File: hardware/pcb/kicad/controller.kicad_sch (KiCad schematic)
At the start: 0 parts

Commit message: feat(hardware): complete reproducible engineering release artifacts
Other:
- note added: "AVL OWNER SIGN-OFF AND PHYSICAL BRING-UP REQUIRED BEFORE POPULATED-BOARD RELEASE"
- note added: "WORKBENCH-1 EVT CARRIER - ARCHITECTURE AND RELEASE GATES"
- note removed: "STOP: SYMBOL CAPTURE, AVL APPROVAL, ERC, ROUTING, DRC AND LAB VALIDATION REQUIRED"
- note removed: "WORKBENCH-1 CONTROLLER - ARCHITECTURE BASELINE - NOT FOR FABRICATION"
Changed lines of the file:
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@@
 (kicad_sch (version 20231120) (generator eeschema)
   (paper "A4")
-  (text "WORKBENCH-1 CONTROLLER - ARCHITECTURE BASELINE - NOT FOR FABRICATION"
+  (text "WORKBENCH-1 EVT CARRIER - ARCHITECTURE AND RELEASE GATES"
     (exclude_from_sim no) (at 105 20 0)
     (effects (font (size 2 2) (thickness 0.3)) (justify bottom)))
@@
     (exclude_from_sim no) (at 105 90 0)
     (effects (font (size 1.5 1.5) (thickness 0.25)) (justify bottom)))
-  (text "STOP: SYMBOL CAPTURE, AVL APPROVAL, ERC, ROUTING, DRC AND LAB VALIDATION REQUIRED"
+  (text "AVL OWNER SIGN-OFF AND PHYSICAL BRING-UP REQUIRED BEFORE POPULATED-BOARD RELEASE"
     (exclude_from_sim no) (at 105 115 0)
     (effects (font (size 1.25 1.25) (thickness 0.2)) (justify bottom)))

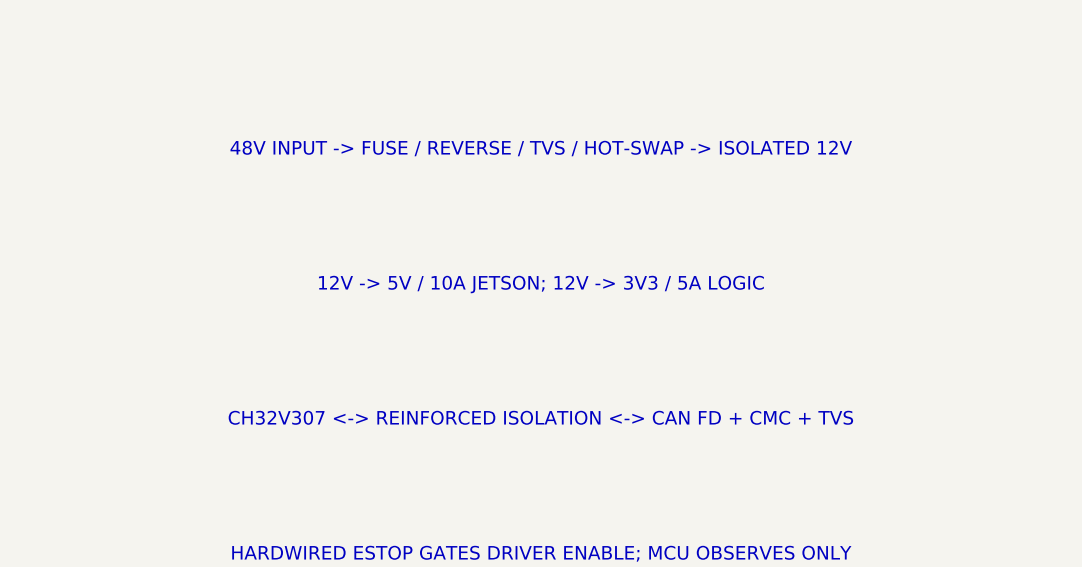
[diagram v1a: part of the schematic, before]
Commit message: feat(hardware): close EVT interface and isolation review
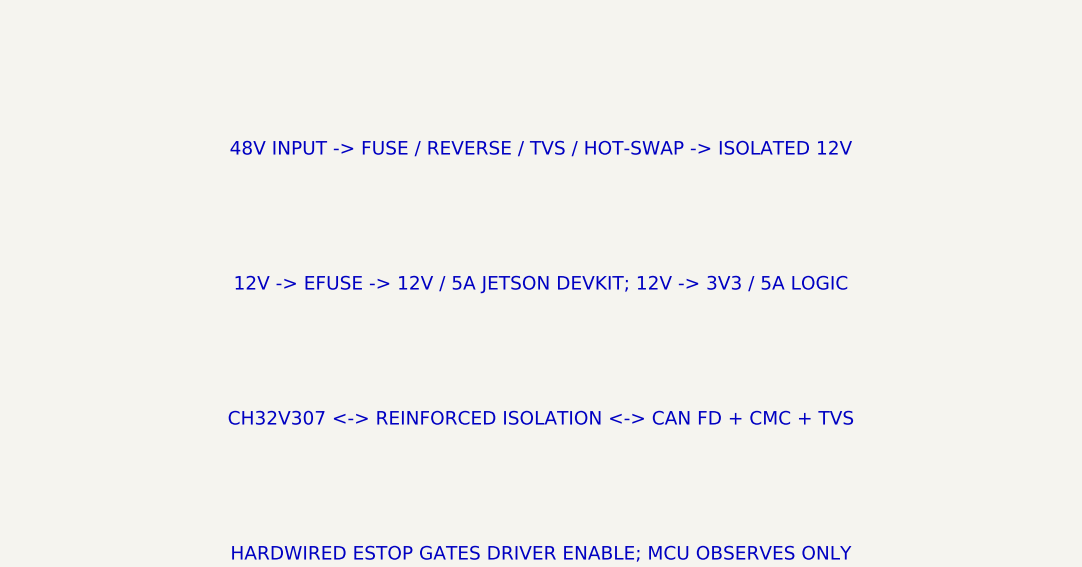
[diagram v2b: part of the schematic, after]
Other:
- note added: "12V -> EFUSE -> 12V / 5A JETSON DEVKIT; 12V -> 3V3 / 5A LOGIC"
- note removed: "12V -> 5V / 10A JETSON; 12V -> 3V3 / 5A LOGIC"
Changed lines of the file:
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@@
     (exclude_from_sim no) (at 105 45 0)
     (effects (font (size 1.5 1.5) (thickness 0.25)) (justify bottom)))
-  (text "12V -> 5V / 10A JETSON; 12V -> 3V3 / 5A LOGIC"
+  (text "12V -> EFUSE -> 12V / 5A JETSON DEVKIT; 12V -> 3V3 / 5A LOGIC"
     (exclude_from_sim no) (at 105 60 0)
     (effects (font (size 1.5 1.5) (thickness 0.25)) (justify bottom)))

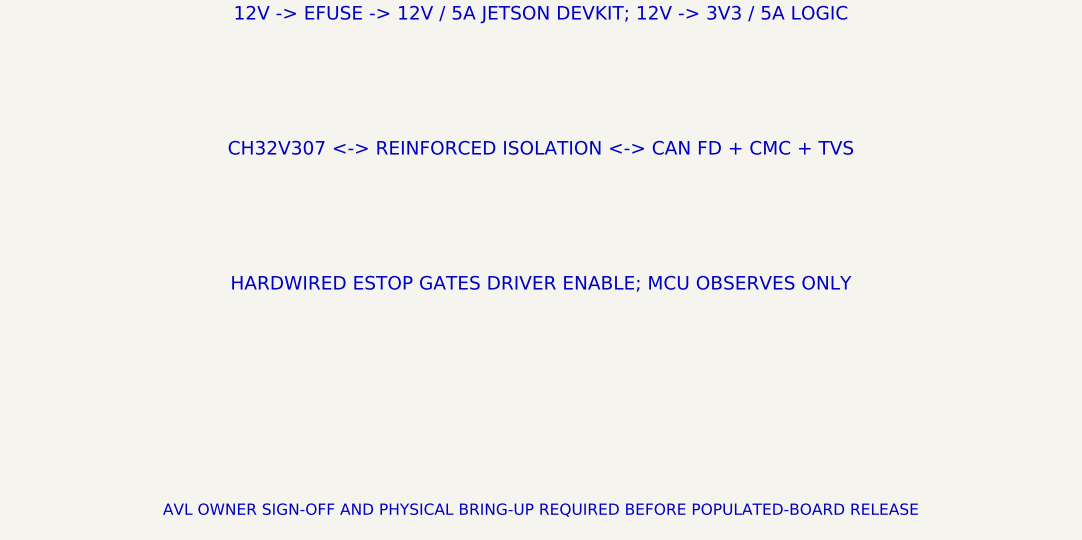
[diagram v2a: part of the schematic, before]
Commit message: feat(hardware): harden safety and order release gates
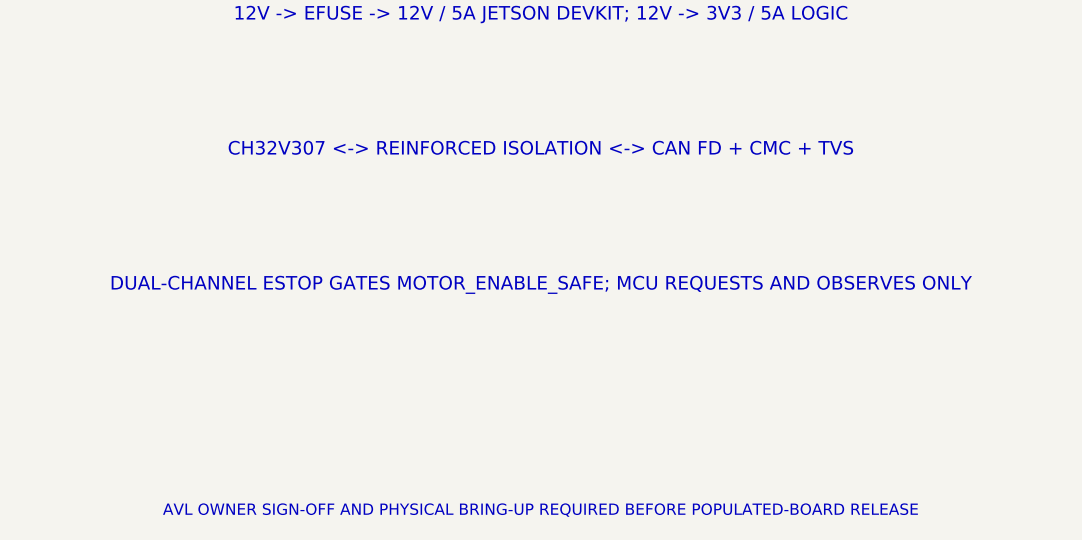
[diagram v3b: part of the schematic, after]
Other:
- note added: "DUAL-CHANNEL ESTOP GATES MOTOR_ENABLE_SAFE; MCU REQUESTS AND OBSERVES ONLY"
- note removed: "HARDWIRED ESTOP GATES DRIVER ENABLE; MCU OBSERVES ONLY"
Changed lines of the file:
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@@
     (exclude_from_sim no) (at 105 75 0)
     (effects (font (size 1.5 1.5) (thickness 0.25)) (justify bottom)))
-  (text "HARDWIRED ESTOP GATES DRIVER ENABLE; MCU OBSERVES ONLY"
+  (text "DUAL-CHANNEL ESTOP GATES MOTOR_ENABLE_SAFE; MCU REQUESTS AND OBSERVES ONLY"
     (exclude_from_sim no) (at 105 90 0)
     (effects (font (size 1.5 1.5) (thickness 0.25)) (justify bottom)))

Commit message: feat(hardware): complete service robot engineering baseline
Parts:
- added C1: 1uF 100V, Capacitor_SMD:C_1210_3225Metric, symbol controller:CAPACITOR
- added C10, C11, C12, C13, C14, C15, C16, C18, C19, C40, C41, C44, C9: 100nF, Capacitor_SMD:C_0603_1608Metric, symbol controller:CAPACITOR
- added C17, C42, C43: 4.7uF, Capacitor_SMD:C_0805_2012Metric, symbol controller:CAPACITOR
- added C2: 10uF 100V, Capacitor_SMD:C_2220_5750Metric, symbol controller:CAPACITOR
- added C20: 1uF 10V, Capacitor_SMD:C_0603_1608Metric, symbol controller:CAPACITOR
- added C3: 470uF 25V, Capacitor_THT:CP_Radial_D12.5mm_P5.00mm, symbol controller:CAPACITOR
- added C4: 1uF 25V, Capacitor_SMD:C_0805_2012Metric, symbol controller:CAPACITOR
- added C5: 220uF 25V, Capacitor_THT:CP_Radial_D10.0mm_P5.00mm, symbol controller:CAPACITOR
- added C6: 22uF 25V, Capacitor_SMD:C_1210_3225Metric, symbol controller:CAPACITOR
- added C7, C8: 47uF 10V, Capacitor_SMD:C_1210_3225Metric, symbol controller:CAPACITOR
- added CG1: 4.7nF 100V, Capacitor_SMD:C_0603_1608Metric, symbol controller:CAPACITOR
- added CSS4: 22nF, Capacitor_SMD:C_0603_1608Metric, symbol controller:CAPACITOR
- added CY1, CY2: 18pF, Capacitor_SMD:C_0603_1608Metric, symbol controller:CAPACITOR
- added D1: SMCJ58A, Diode_SMD:D_SMC, symbol controller:DIODE
- added D2: CAN FD TVS, WB:CAN_TVS, symbol controller:CAN_TVS
- added D3, D4: FLYBACK, Diode_SMD:D_SOD-123, symbol controller:DIODE
- added F1: 10A 125V, WB:Fuse_4510, symbol controller:FUSE
- added F2: PTC 0.25A, Fuse:Fuse_1206_3216Metric, symbol controller:FUSE
- added J1: 48V INPUT, WB:MicroFit_2x2, symbol controller:CONN_4
- added J10: DUAL ESTOP LOOP, WB:MicroFit_2x2, symbol controller:CONN_4
- added J11: SAFETY OUTPUT, WB:MicroFit_2x2, symbol controller:CONN_4
- added J12: DUAL MANUAL RESET, WB:MicroFit_2x2, symbol controller:CONN_4
- added J13: WCH DEBUG, Connector_PinHeader_2.54mm:PinHeader_1x04_P2.54mm_Vertical, symbol controller:CONN_4
- added J2: 12V MOTOR AUX, WB:MicroFit_2x2, symbol controller:CONN_4
- added J3: JETSON DEVKIT 12V, WB:MicroFit_2x2, symbol controller:CONN_4
- added J4: JETSON MCU BACKPLANE, Connector_PinHeader_2.54mm:PinHeader_2x10_P2.54mm_Vertical, symbol controller:CONN_20
- added J5: CAN A, WB:MicroFit_2x2, symbol controller:CONN_4
- added J6: CAN B, WB:MicroFit_2x2, symbol controller:CONN_4
- added JP1: CAN TERM, Connector_PinHeader_2.54mm:PinHeader_1x02_P2.54mm_Vertical, symbol controller:CONN_2
- added K1: FORCE-GUIDED 12V A, WB:Panasonic_SFM4, symbol controller:SFM4_RELAY
- added K2: FORCE-GUIDED 12V B, WB:Panasonic_SFM4, symbol controller:SFM4_RELAY
- added L1: 100R@100MHz, WB:ACT45B, symbol controller:CAN_CMC
- added Q1, Q2: 150V N-MOS, Package_SON:Infineon_PG-TDSON-8_6.15x5.15mm, symbol controller:NMOS
- added R30, R31, R32, R33, R34, R35, R36, R37, R38, R39, R40, R41, R42: 33R, Resistor_SMD:R_0603_1608Metric, symbol controller:RESISTOR
- added R43, R44, R45, R46, R57: 100k, Resistor_SMD:R_0603_1608Metric, symbol controller:RESISTOR
- added R47, R49, R50, R51, R54, RPG3: 10k, Resistor_SMD:R_0603_1608Metric, symbol controller:RESISTOR
- added R48: 3.00k 1%, Resistor_SMD:R_0603_1608Metric, symbol controller:RESISTOR
- added R52, R53, R55, R56: 4.7k, Resistor_SMD:R_0603_1608Metric, symbol controller:RESISTOR
- added R58: 120R 1%, Resistor_SMD:R_1206_3216Metric, symbol controller:RESISTOR
- added R59: 73.2k 1%, Resistor_SMD:R_0603_1608Metric, symbol controller:RESISTOR
- added R60, RFB2: 10.0k 1%, Resistor_SMD:R_0603_1608Metric, symbol controller:RESISTOR
- added RFB1: 45.0k 1%, Resistor_SMD:R_0603_1608Metric, symbol controller:RESISTOR
- added RG1: 22k, Resistor_SMD:R_0603_1608Metric, symbol controller:RESISTOR
- added RPG1: 453k 1%, Resistor_SMD:R_0603_1608Metric, symbol controller:RESISTOR
- added RPG2: 56.0k 1%, Resistor_SMD:R_0603_1608Metric, symbol controller:RESISTOR
- added RS1: 6mR 3W 1%, WB:Sense_3637, symbol controller:RESISTOR
- added RSH1: 510k, Resistor_SMD:R_0603_1608Metric, symbol controller:RESISTOR
- added RUV1: 19.6M 1%, Resistor_SMD:R_1206_3216Metric, symbol controller:RESISTOR
- added RUV2: 133k 1%, Resistor_SMD:R_0603_1608Metric, symbol controller:RESISTOR
- added RUV3: 162k 1%, Resistor_SMD:R_0603_1608Metric, symbol controller:RESISTOR
- added TP1: VBAT_PROTECTED, TestPoint:TestPoint_Pad_D1.5mm, symbol controller:TESTPOINT
- added TP2: 12V_ISO, TestPoint:TestPoint_Pad_D1.5mm, symbol controller:TESTPOINT
- added TP3: JETSON_12V, TestPoint:TestPoint_Pad_D1.5mm, symbol controller:TESTPOINT
- added TP4: 3V3_LOGIC, TestPoint:TestPoint_Pad_D1.5mm, symbol controller:TESTPOINT
- added TP5: GND, TestPoint:TestPoint_Pad_D1.5mm, symbol controller:TESTPOINT
- added TP6: CANH, TestPoint:TestPoint_Pad_D1.5mm, symbol controller:TESTPOINT
- added TP7: CANL, TestPoint:TestPoint_Pad_D1.5mm, symbol controller:TESTPOINT
- added TP8: MCU_RESET, TestPoint:TestPoint_Pad_D1.5mm, symbol controller:TESTPOINT
- added U1: LTC4368HMS-2, Package_SO:MSOP-10_3x3mm_P0.5mm, symbol controller:LTC4368
- added U2: ISOLATED 48V-12V 240W (TBD), WB:Isolated_48V_12V_240W_TBD, symbol controller:ISOLATED_DC_DC_TBD
- added U3: TPS26633RGE, WB:TPS26633_RGE24, symbol controller:TPS26633RGE
- added U4: RPL-5.0 3V3/5A, WB:RPL-5.0_QFN24, symbol controller:RPL_5_0
- added U5: CH32V307VCT6, Package_QFP:LQFP-100_14x14mm_P0.5mm, symbol controller:CH32V307VCT6
- added U6: ISO1042DW, WB:ISO1042_DW16_HV, symbol controller:ISO1042DW
- added U7: 3V3-5V ISO 1W, Converter_DCDC:Converter_DCDC_muRata_MEJ1SxxxxSC_THT, symbol controller:MEJ1S0305SC
- added U8: ESTOP DIAGNOSTIC OPTO, Package_SO:SOIC-16W_7.5x10.3mm_P1.27mm, symbol controller:TLP293_4
- added Y1: 8MHz, Crystal:Crystal_SMD_3225-4Pin_3.2x2.5mm, symbol controller:CRYSTAL
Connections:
- new net 12V_ISO: C3.1 (+), C4.1 (+), C6.1 (+), F2.1 (IN), J2.1, J2.2, R46.1, R59.1, TP2.1 (TP), U2.4 (+OUT), U3.1 (IN), U3.2 (IN), U3.5 (IN_SYS), U4.22 (VIN)
- new net 3V3_LOGIC: C10.1 (+), C11.1 (+), C12.1 (+), C13.1 (+), C14.1 (+), C15.1 (+), C16.1 (+), C17.1 (+), C40.1 (+), C42.1 (+), C7.1 (+), C8.1 (+), C9.1 (+), J11.4, J13.1, J4.1, J4.3, K1.5 (SENSE_COM), K1.9 (EDM_COM), K2.9 (EDM_COM), R47.1, R49.1, R50.1, R54.1, R55.1, R56.1, RFB1.1, RPG3.1, TP4.1 (TP), U3.12 (SHDN), U4.10 (VOUT), U4.11 (VOUT), U4.12 (VOUT), U4.9 (VOUT), U5.100 (VIO), U5.11 (VDD), U5.21 (VREF+), U5.22 (VDDA), U5.28 (VDD), U5.50 (VIO), U5.6 (VBAT), U5.75 (VDD), U6.1 (VCC1), U7.1 (+VIN)
- new net 3V3_PGOOD: U4.20 (PG), U4.21 (PG)
- new net 5V_CAN_ISO: C41.1 (+), C43.1 (+), C44.1 (+), U6.11 (VCC2), U6.16 (VCC2), U7.7 (+VOUT)
- new net BOOT0: R43.1, U5.94 (BOOT0)
- new net CANH: D2.1 (CANH), J5.1, J6.1, L1.4 (CANH_OUT), R58.1, TP6.1 (TP)
- new net CANH_RAW: L1.1 (CANH_IN), U6.13 (CANH)
- new net CANL: D2.2 (CANL), J5.2, J6.2, JP1.2, L1.3 (CANL_OUT), TP7.1 (TP)
- new net CANL_RAW: L1.2 (CANL_IN), U6.12 (CANL)
- new net CAN_RX: U5.81 (PD0/CAN1_RX), U6.5 (RXD)
- new net CAN_TERM: JP1.1, R58.2
- new net CAN_TX: U5.82 (PD1/CAN1_TX), U6.3 (TXD)
- new net ESTOP_12V: F2.2 (OUT), J10.1, J10.3
- new net ESTOP_A_MON: R49.2, U5.57 (PD10), U8.16 (C1)
- new net ESTOP_B_MON: R50.2, U5.58 (PD11), U8.14 (C2)
- new net ESTOP_CH_A_RETURN: J10.2, J12.1, K1.7 (HOLD_COM), U8.1 (A1)
- new net ESTOP_CH_B_RETURN: J10.4, J12.3, K2.7 (HOLD_COM), U8.3 (A2)
- new net ESTOP_SENSE: J11.2, J4.17, K2.6 (SENSE_NO), R57.1, U5.54 (PB15)
- new net FET_COMMON: CG1.2 (-), Q1.2 (S), Q2.2 (S)
- new net FET_GATE: CG1.1 (+), Q1.1 (G), Q2.1 (G), RG1.2
- new net GND: C10.2 (-), C11.2 (-), C12.2 (-), C13.2 (-), C14.2 (-), C15.2 (-), C16.2 (-), C17.2 (-), C18.2 (-), C19.2 (-), C20.2 (-), C3.2 (-), C4.2 (-), C40.2 (-), C42.2 (-), C5.2 (-), C6.2 (-), C7.2 (-), C8.2 (-), C9.2 (-), CSS4.2 (-), CY1.2 (-), CY2.2 (-), D3.2 (A), D4.2 (A), J11.3, J13.4, J2.3, J2.4, J3.3, J3.4, J4.2, J4.4, K1.2 (COIL-), K2.2 (COIL-), R43.2, R44.2, R45.2, R48.2, R51.2, R52.2, R53.2, R57.2, R60.2, RFB2.2, RPG2.2, TP5.1 (TP), U2.5 (-OUT), U3.25 (PowerPAD), U3.7 (PLIM), U3.8 (GND), U4.1 (PGND), U4.18 (AGND), U4.2 (PGND), U4.24 (PGND), U4.3 (PGND), U4.4 (PGND), U4.5 (PGND), U5.10 (VSS), U5.19 (VSSA), U5.20 (VREF-), U5.27 (VSS), U5.49 (VSS), U5.74 (VSS), U5.99 (VSS), U6.2 (GND1), U6.8 (GND1), U7.2 (-VIN), U8.13 (E2), U8.15 (E1)
- new net GND_CAN_ISO: C41.2 (-), C43.2 (-), C44.2 (-), D2.3 (GND), D2.4 (GND), J5.3, J6.3, U6.10 (GND2), U6.15 (GND2), U6.9 (GND2), U7.5 (-VOUT)
- new net GND_PWR: C1.2 (-), C2.2 (-), D1.2 (A), J1.3, J1.4, RUV3.2, U1.1 (GND), U1.2 (RETRY), U2.2 (-IN)
- new net I2C_SCL: J4.16, R39.2, R55.2
- new net I2C_SCL_MCU: R39.1, U5.92 (PB6/I2C1_SCL)
- new net I2C_SDA: J4.15, R40.2, R56.2
- new net I2C_SDA_MCU: R40.1, U5.93 (PB7/I2C1_SDA)
- new net INPUT_SENSE: Q2.3 (D), RS1.1, U1.9 (SENSE)
- new net JETSON_12V: C5.1 (+), J3.1, J3.2, RPG1.1, TP3.1 (TP), U3.17 (OUT), U3.18 (OUT)
- new net JETSON_ENABLE_REQ: J4.8, U5.91 (PB5)
- new net JETSON_FAULT_N: R47.2, U3.14 (FLT)
- new net JETSON_PGOOD: RPG3.2, U3.16 (PGOOD)
- new net MCU_RESET: C19.1 (+), J4.20, R54.2, TP8.1 (TP), U5.14 (NRST)
- new net MOTOR_CS0: J4.9, R33.2
- new net MOTOR_CS0_MCU: R33.1, U5.35 (PB0)
- new net MOTOR_CS1: J4.10, R34.2
- new net MOTOR_CS1_MCU: R34.1, U5.36 (PB1)
- new net MOTOR_CS2: J4.11, R35.2
- new net MOTOR_CS2_MCU: R35.1, U5.47 (PB10)
- new net MOTOR_CS3: J4.12, R36.2
- new net MOTOR_CS3_MCU: R36.1, U5.48 (PB11)
- new net MOTOR_CS4: J4.13, R37.2
- new net MOTOR_CS4_MCU: R37.1, U5.51 (PB12)
- new net MOTOR_CS5: J4.14, R38.2
- new net MOTOR_CS5_MCU: R38.1, U5.52 (PB13)
- new net MOTOR_ENABLE_REQ: K1.3 (SAFE_COM), U5.53 (PB14)
- new net MOTOR_ENABLE_SAFE: J11.1, K2.4 (SAFE_NO)
- new net OSC_IN: CY1.1 (+), U5.12 (OSC_IN), Y1.1
- new net OSC_OUT: CY2.1 (+), U5.13 (OSC_OUT), Y1.2
- new net OV_SET: RUV2.2, RUV3.1, U1.3 (OV)
- new net RELAY_A_NC: K1.10 (EDM_NC), R44.1, U5.55 (PD8)
- new net RELAY_B_NC: K2.10 (EDM_NC), R45.1, U5.56 (PD9)
- new net RESET_CH_A_RETURN: D3.1 (K), J12.2, K1.1 (COIL+), K1.8 (HOLD_NO)
- new net RESET_CH_B_RETURN: D4.1 (K), J12.4, K2.1 (COIL+), K2.8 (HOLD_NO)
- new net SAFE_STAGE_A: K1.4 (SAFE_NO), K2.3 (SAFE_COM)
- new net SENSE_STAGE_A: K1.6 (SENSE_NO), K2.5 (SENSE_COM)
- new net SPI_MISO: J4.7, R32.2
- new net SPI_MISO_MCU: R32.1, U5.31 (PA6/SPI1_MISO)
- new net SPI_MOSI: J4.6, R31.2
- new net SPI_MOSI_MCU: R31.1, U5.32 (PA7/SPI1_MOSI)
- new net SPI_SCLK: J4.5, R30.2
- new net SPI_SCLK_MCU: R30.1, U5.30 (PA5/SPI1_SCK)
- new net SWCLK: J13.3, U5.76 (SWCLK)
- new net SWDIO: J13.2, U5.72 (SWDIO)
- new net U1_GATE: RG1.1, U1.10 (GATE)
- new net U1_SHDN: RSH1.2, U1.6 (SHDN)
- new net U3_DVDT: C18.1 (+), U3.9 (dVdT)
- new net U3_ILIM: R48.1, U3.10 (ILIM)
- new net U3_IMON: R51.1, U3.13 (IMON)
- new net U3_PGTH: RPG1.2, RPG2.1, U3.15 (PGTH)
- new net U3_UVLO: R59.2, R60.1, U3.6 (UVLO)
- new net U4_CTRL: R46.2, U4.16 (CTRL)
- new net U4_FB: RFB1.2, RFB2.1, U4.17 (FB)
- new net U4_SS: CSS4.1 (+), U4.19 (SS)
- new net U4_VCC: C20.1 (+), U4.6 (VCC)
- new net U8_LED_A_K: R52.1, U8.2 (K1)
- new net U8_LED_B_K: R53.1, U8.4 (K2)
- new net UART_RX: J4.19, R42.2
- new net UART_RX_MCU: R42.1, U5.69 (PA10/USART1_RX)
- new net UART_TX: J4.18, R41.2
- new net UART_TX_MCU: R41.1, U5.68 (PA9/USART1_TX)
- new net UV_SET: RUV1.2, RUV2.1, U1.4 (UV)
- new net VBAT_FUSED: D1.1 (K), F1.2 (OUT), Q1.3 (D), RSH1.1, RUV1.1, U1.5 (VIN)
- new net VBAT_PROTECTED: C1.1 (+), C2.1 (+), RS1.2, TP1.1 (TP), U1.8 (VOUT), U2.1 (+IN)
- new net VBAT_RAW: F1.1 (IN), J1.1, J1.2
- no-connect marks 0 -> 92
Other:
- note added: "3V3 POWER"
- note added: "HARDWIRED ESTOP"
- note added: "INPUT PROTECTION"
- note added: "ISOLATED CAN FD"
- note added: "ISOLATED POWER"
- note added: "JETSON EFUSE"
- note added: "MCU AND BACKPLANE"
- note added: "POWER OUTPUTS"
- note added: "TEST ACCESS"
- note removed: "12V -> EFUSE -> 12V / 5A JETSON DEVKIT; 12V -> 3V3 / 5A LOGIC"
- note removed: "48V INPUT -> FUSE / REVERSE / TVS / HOT-SWAP -> ISOLATED 12V"
- note removed: "AVL OWNER SIGN-OFF AND PHYSICAL BRING-UP REQUIRED BEFORE POPULATED-BOARD RELEASE"
- note removed: "CH32V307 <-> REINFORCED ISOLATION <-> CAN FD + CMC + TVS"
- note removed: "DUAL-CHANNEL ESTOP GATES MOTOR_ENABLE_SAFE; MCU REQUESTS AND OBSERVES ONLY"
- note removed: "WORKBENCH-1 EVT CARRIER - ARCHITECTURE AND RELEASE GATES"
- company: (none) -> Workbench-1
- title: (none) -> Workbench-1 controller EVT detailed schematic
